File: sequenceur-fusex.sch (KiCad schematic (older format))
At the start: 29 parts, among them J1 ALIM 12v, J2 ELECTRO AIMANT PERMANANT, J3 JACK M/A NF, J4 JACK DEP NF, U1 LM324

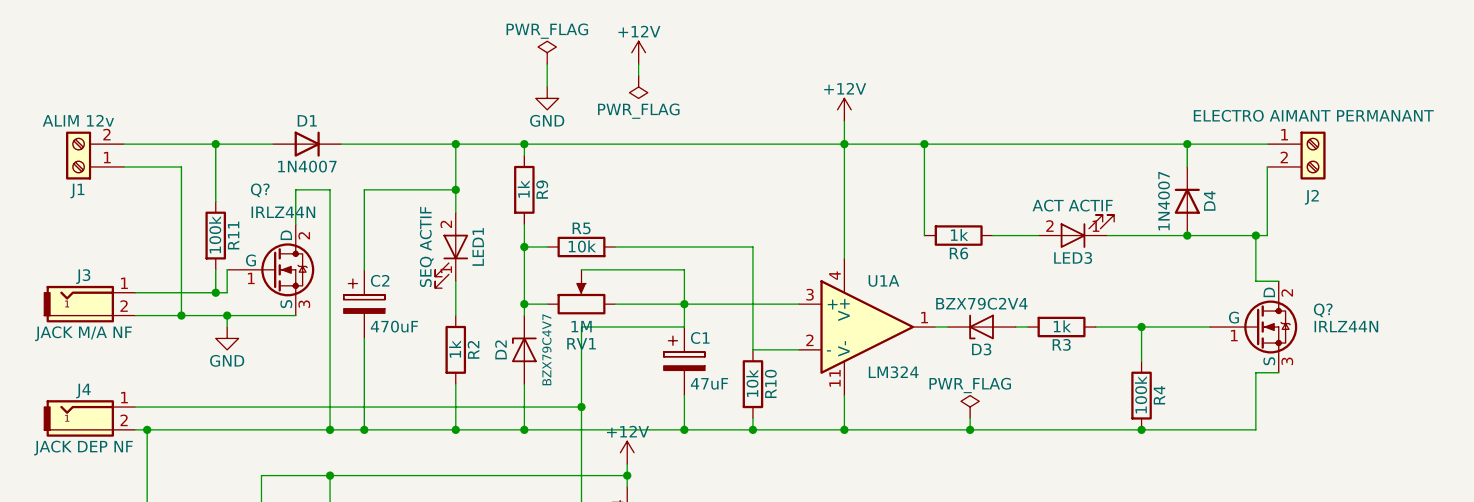
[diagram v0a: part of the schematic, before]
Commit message: add a fuse and enlarge some track
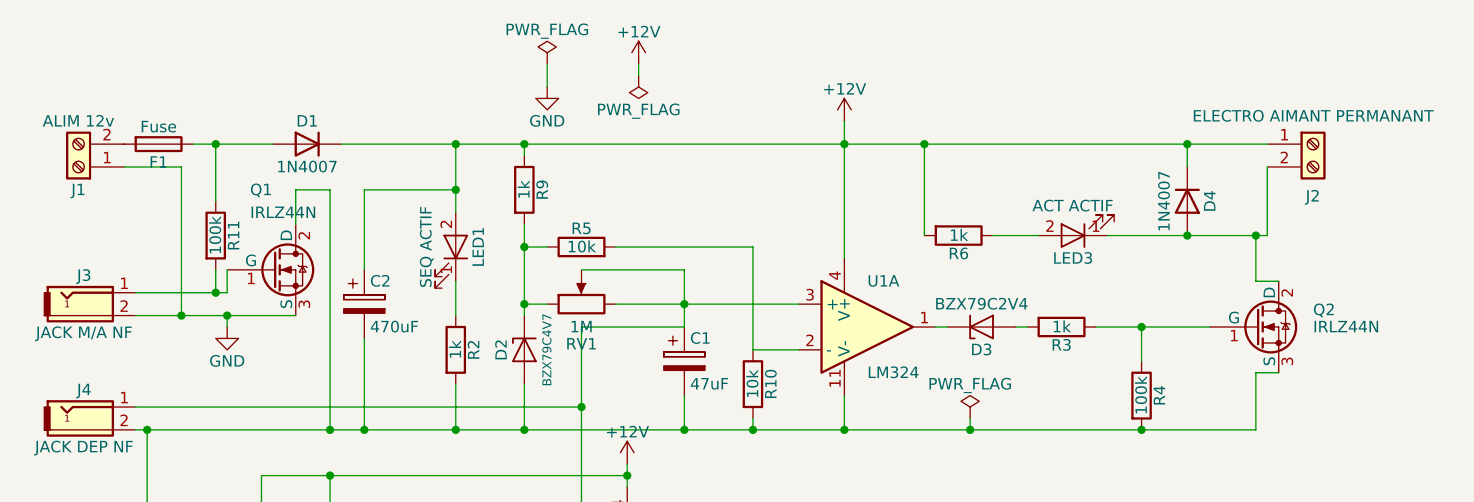
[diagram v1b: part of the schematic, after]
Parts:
- added F1: Fuse, fuse:NANO2_SMD, symbol Fuse
- gave numbers to parts that had none: 2
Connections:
- net at D1.2 (A), R11.1: now also F1.1; no longer J1.2 (Pin_2)
- new net: F1.2, J1.2 (Pin_2)
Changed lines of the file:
@@
 $EndComp
 $Comp
-L IRLZ44N Q?
+L IRLZ44N Q1
 U 1 1 5B01B738
 P 2100 2350
-F 0 "Q?" H 2000 2700 50  0000 L CNN
+F 0 "Q1" H 2000 2700 50  0000 L CNN
 F 1 "IRLZ44N" H 2000 2600 50  0000 L CNN
 F 2 "TO_SOT_Packages_THT:TO-220_Vertical" H 2350 2275 50  0001 L CIN
@@
 $EndComp
 $Comp
-L IRLZ44N Q?
+L IRLZ44N Q2
 U 1 1 5B01B84F
 P 6400 2600
-F 0 "Q?" H 6650 2675 50  0000 L CNN
+F 0 "Q2" H 6650 2675 50  0000 L CNN
 F 1 "IRLZ44N" H 6650 2600 50  0000 L CNN
 F 2 "TO_SOT_Packages_THT:TO-220_Vertical" H 6650 2525 50  0001 L CIN
@@
 $EndComp
 Wire Wire Line
-	1450 1800 2100 1800
-Wire Wire Line
 	1850 1800 1850 2050
 Wire Wire Line
@@
 Wire Wire Line
 	2200 2000 2350 2000
+$Comp
+L Fuse F1
+U 1 1 5B18123E
+P 1600 1800
+F 0 "F1" V 1680 1800 50  0000 C CNN
+F 1 "Fuse" V 1525 1800 50  0000 C CNN
+F 2 "fuse:NANO2_SMD" V 1530 1800 50  0001 C CNN
+F 3 "" H 1600 1800 50  0001 C CNN
+	1    1600 1800
+	0    1    1    0
+$EndComp
+Wire Wire Line
+	1750 1800 2100 1800
 $EndSCHEMATC

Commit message: select smt instead of though-holes
update symbol and cache file for kicadv5

delete net list
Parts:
- C1: footprint Capacitors_THT:CP_Radial_D6.3mm_P2.50mm -> Capacitor_SMD:CP_Elec_6.3x5.8; symbol CP -> sequenceur-fusex-rescue:CP-sequenceur-fusex-rescue-sequenceur-fusex-rescue-sequenceur-fusex-rescue
- C2: footprint Capacitors_THT:CP_Radial_D10.0mm_P5.00mm -> Capacitor_SMD:CP_Elec_10x10.5; symbol CP -> sequenceur-fusex-rescue:CP-sequenceur-fusex-rescue-sequenceur-fusex-rescue-sequenceur-fusex-rescue
- C3: footprint Capacitors_SMD:C_0805_HandSoldering -> Capacitor_SMD:C_0805_2012Metric_Pad1.18x1.45mm_HandSolder; symbol C -> sequenceur-fusex-rescue:C-sequenceur-fusex-rescue-sequenceur-fusex-rescue-sequenceur-fusex-rescue
- D1, D4: footprint Diodes_THT:D_DO-41_SOD81_P7.62mm_Horizontal -> Diode_SMD:D_SMA_Handsoldering; symbol 1N4007 -> Diode:1N4007
- D2: footprint Diodes_THT:D_T-1_P5.08mm_Horizontal -> Diode_SMD:D_SOD-523; symbol D_Zener -> sequenceur-fusex-rescue:D_Zener-sequenceur-fusex-rescue-sequenceur-fusex-rescue-sequenceur-fusex-rescue
- D3: footprint Diodes_THT:D_T-1_P5.08mm_Horizontal -> Diode_SMD:D_SOD-123; symbol D_Zener -> sequenceur-fusex-rescue:D_Zener-sequenceur-fusex-rescue-sequenceur-fusex-rescue-sequenceur-fusex-rescue
- F1: footprint fuse:NANO2_SMD -> Fuse:Fuse_Littelfuse-NANO2-451_453; symbol Fuse -> sequenceur-fusex-rescue:Fuse-sequenceur-fusex-rescue-sequenceur-fusex-rescue-sequenceur-fusex-rescue
- J1, J2: footprint Connectors_Terminal_Blocks:TerminalBlock_bornier-2_P5.08mm -> TerminalBlock:TerminalBlock_bornier-2_P5.08mm; symbol Screw_Terminal_01x02 -> sequenceur-fusex-rescue:Screw_Terminal_01x02-sequenceur-fusex-rescue-sequenceur-fusex-rescue-sequenceur-fusex-rescue
- J3, J4: footprint (none) -> TerminalBlock:TerminalBlock_bornier-2_P5.08mm; symbol Audio-Jack-2 -> sequenceur-fusex-rescue:Audio-Jack-2-sequenceur-fusex-rescue-sequenceur-fusex-rescue-sequenceur-fusex-rescue
- LED1, LED2, LED3: footprint LEDs:LED_0805_HandSoldering -> LED_SMD:LED_0805_2012Metric_Pad1.15x1.40mm_HandSolder; symbol LED -> sequenceur-fusex-rescue:LED-sequenceur-fusex-rescue-sequenceur-fusex-rescue-sequenceur-fusex-rescue
- Q1, Q2: footprint TO_SOT_Packages_THT:TO-220_Vertical -> Package_TO_SOT_SMD:TO-263-3_TabPin2; symbol IRLZ44N -> sequenceur-fusex-rescue:IRLZ44N-sequenceur-fusex-rescue-sequenceur-fusex-rescue-sequenceur-fusex-rescue
- R1, R10, R11, R2, R3, R4, R5, R6, R7, R8, R9: footprint Resistors_SMD:R_0805_HandSoldering -> Resistor_SMD:R_0805_2012Metric_Pad1.20x1.40mm_HandSolder; symbol R -> sequenceur-fusex-rescue:R-sequenceur-fusex-rescue-sequenceur-fusex-rescue-sequenceur-fusex-rescue
- RV1: footprint Potentiometers:Potentiometer_Alps_RK097_Single_Vertical -> SmacSys:3313J1102E; symbol POT -> sequenceur-fusex-rescue:POT-sequenceur-fusex-rescue-sequenceur-fusex-rescue-sequenceur-fusex-rescue
- U1: footprint Housings_DIP:DIP-14_W7.62mm_LongPads -> Package_SO:SOIC-14_3.9x8.7mm_P1.27mm; symbol LM324 -> sequenceur-fusex-rescue:LM324-sequenceur-fusex-rescue-sequenceur-fusex-rescue-sequenceur-fusex-rescue
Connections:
- net at C1.2, C2.2, C3.2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: now also U1.5 (+)
- net at C1.1, J4.1, RV1.2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: no longer U1.5 (+)
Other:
- moved on the sheet: C1, C2, C3, D1, D2, D3, D4, F1, J1, J2, J3, J4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
